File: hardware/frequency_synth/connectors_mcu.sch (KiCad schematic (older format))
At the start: 0 parts

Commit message: finished initial schematic of synth module
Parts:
- added D?: LED, LEDs:LED_0603, symbol LED
- added P? (x2): CONN_01X02, Terminal_Blocks:TerminalBlock_Pheonix_PT-3.5mm_2pol, symbol CONN_01X02
- added R?: 10k, Resistors_SMD:R_0603, symbol R_Small
- added U?: boosterpack_ti, vna_footprints:ti_booster40, symbol boosterpack_ti
- added U?: CONN_SMA, vna_footprints:732512200_SMA, symbol CONN_SMA
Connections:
- net labels added: +3V3, +5V, 3V3, 5V, ADF_CE_0, ADF_CLK_0, ADF_DATA_0, ADF_LE_0, ADF_LOCK_0, ATT_1, ATT_2, ATT_3, ATT_4, ATT_5, ATT_6, FILTA, FILTA_0, FILTB, FILTB_0, FILTC, FILTC_0, GND, LMX_CE, LMX_CLK, LMX_DAT, LMX_LE, LMX_LOCK, POWERDET, REF_CE, REF_OE, REF_SCL, REF_SDA, RFSW, RFSW_0, RFSW_1, RFSW_2, SYNTH_OUT, VCC
- wire segments 0 -> 64
- no-connect marks 0 -> 2
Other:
- note added: "filter bank"
- note added: "rf switch control"

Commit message: reducing component values across module, synth schematic cleanups
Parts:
- removed U?: CONN_SMA, vna_footprints:732512200_SMA, symbol CONN_SMA
- added U?: CONN_SMA_2GND, symbol CONN_SMA_2GND
- R55: renamed from R?; footprint Resistors_SMD:R_0603 -> Resistors_SMD:R_0402
- gave numbers to parts that had none: 4
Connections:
- wire segments 64 -> 62
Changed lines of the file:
@@
 LIBS:74hc04
 LIBS:74hc04_full
+LIBS:conn_sma_2gnd
 LIBS:frequency_synth-cache
-LIBS:boosterpack-cache
-LIBS:refclk_breakout-cache
 EELAYER 25 0
 EELAYER END
@@
 $EndDescr
 $Comp
-L boosterpack_ti U?
+L boosterpack_ti U17
 U 1 1 572E0ED9
 P 1950 2850
-F 0 "U?" H 1700 4450 60  0000 C CNN
+F 0 "U17" H 1700 4450 60  0000 C CNN
 F 1 "boosterpack_ti" H 1950 4250 60  0000 C CNN
 F 2 "vna_footprints:ti_booster40" H 1700 4450 60  0001 C CNN
@@
 $EndComp
 $Comp
-L GND #PWR?
+L GND #PWR213
 U 1 1 572E0EDA
 P 2650 2950
-F 0 "#PWR?" H 2650 2700 50  0001 C CNN
+F 0 "#PWR213" H 2650 2700 50  0001 C CNN
 F 1 "GND" H 2650 2800 50  0000 C CNN
 F 2 "" H 2650 2950 50  0000 C CNN
@@
 $EndComp
 $Comp
-L GND #PWR?
+L GND #PWR214
 U 1 1 572E0EDB
 P 2700 1850
-F 0 "#PWR?" H 2700 1600 50  0001 C CNN
+F 0 "#PWR214" H 2700 1600 50  0001 C CNN
 F 1 "GND" H 2700 1700 50  0000 C CNN
 F 2 "" H 2700 1850 50  0000 C CNN
@@
 $EndComp
 $Comp
-L CONN_01X02 P?
+L CONN_01X02 P1
 U 1 1 572E0EDE
 P 6050 1150
-F 0 "P?" H 6050 1300 50  0000 C CNN
+F 0 "P1" H 6050 1300 50  0000 C CNN
 F 1 "CONN_01X02" V 6150 1150 50  0000 C CNN
 F 2 "Terminal_Blocks:TerminalBlock_Pheonix_PT-3.5mm_2pol" H 6050 1150 50  0001 C CNN
@@
 $EndComp
 $Comp
-L GND #PWR?
+L GND #PWR218
 U 1 1 572E0EDF
 P 6000 1450
-F 0 "#PWR?" H 6000 1200 50  0001 C CNN
+F 0 "#PWR218" H 6000 1200 50  0001 C CNN
 F 1 "GND" H 6000 1300 50  0000 C CNN
 F 2 "" H 6000 1450 50  0000 C CNN
@@
 FILTC_0
 $Comp
-L GND #PWR?
+L GND #PWR222
 U 1 1 572E0EEC
 P 9800 1200
-F 0 "#PWR?" H 9800 950 50  0001 C CNN
+F 0 "#PWR222" H 9800 950 50  0001 C CNN
 F 1 "GND" H 9800 1050 50  0000 C CNN
 F 2 "" H 9800 1200 50  0000 C CNN
@@
 $EndComp
 $Comp
-L +5V #PWR?
+L +5V #PWR223
 U 1 1 572E0EEE
 P 9850 1300
-F 0 "#PWR?" H 9850 1150 50  0001 C CNN
+F 0 "#PWR223" H 9850 1150 50  0001 C CNN
 F 1 "+5V" H 9850 1440 50  0000 C CNN
 F 2 "" H 9850 1300 50  0000 C CNN
@@
 FILTC_0
 $Comp
-L LED D?
+L LED D9
 U 1 1 572E0F0F
 P 5300 1100
-F 0 "D?" H 5300 1200 50  0000 C CNN
+F 0 "D9" H 5300 1200 50  0000 C CNN
 F 1 "LED" H 5300 1000 50  0000 C CNN
 F 2 "LEDs:LED_0603" H 5300 1100 50  0001 C CNN
@@
 $EndComp
 $Comp
-L R_Small R?
+L R_Small R55
 U 1 1 572E0F10
 P 5300 1500
-F 0 "R?" H 5330 1520 50  0000 L CNN
+F 0 "R55" H 5330 1520 50  0000 L CNN
 F 1 "10k" H 5330 1460 50  0000 L CNN
-F 2 "Resistors_SMD:R_0603" H 5300 1500 50  0001 C CNN
+F 2 "Resistors_SMD:R_0402" H 5300 1500 50  0001 C CNN
 F 3 "" H 5300 1500 50  0000 C CNN
 	1    5300 1500
@@
 $EndComp
 $Comp
-L VCC #PWR?
+L VCC #PWR216
 U 1 1 572E0F11
 P 5300 800
-F 0 "#PWR?" H 5300 650 50  0001 C CNN
+F 0 "#PWR216" H 5300 650 50  0001 C CNN
 F 1 "VCC" H 5300 950 50  0000 C CNN
 F 2 "" H 5300 800 50  0000 C CNN
@@
 $EndComp
 $Comp
-L GND #PWR?
+L GND #PWR217
 U 1 1 572E0F12
 P 5300 1700
-F 0 "#PWR?" H 5300 1450 50  0001 C CNN
+F 0 "#PWR217" H 5300 1450 50  0001 C CNN
 F 1 "GND" H 5300 1550 50  0000 C CNN
 F 2 "" H 5300 1700 50  0000 C CNN
@@
 POWERDET
 $Comp
-L CONN_SMA U?
-U 1 1 572E0F13
-P 4700 4700
-F 0 "U?" H 4350 4900 60  0000 C CNN
-F 1 "CONN_SMA" H 4550 5050 60  0000 C CNN
-F 2 "vna_footprints:732512200_SMA" H 4700 4700 60  0001 C CNN
-F 3 "" H 4700 4700 60  0000 C CNN
-	1    4700 4700
-	1    0    0    -1
-$EndComp
-$Comp
-L GND #PWR?
+L GND #PWR215
 U 1 1 572E0F14
 P 4550 5300
-F 0 "#PWR?" H 4550 5050 50  0001 C CNN
+F 0 "#PWR215" H 4550 5050 50  0001 C CNN
 F 1 "GND" H 4550 5150 50  0000 C CNN
 F 2 "" H 4550 5300 50  0000 C CNN
@@
 Text HLabel 3400 4700 0    60   Input ~ 0
 SYNTH_OUT
-Connection ~ 4750 5250
-Wire Wire Line
-	4750 5150 4750 5250
-Connection ~ 4650 5250
 Wire Wire Line
 	4650 5150 4650 5250
 Connection ~ 4550 5250
 Wire Wire Line
-	4550 5250 4850 5250
-Wire Wire Line
-	4850 5250 4850 5150
-Wire Wire Line
 	4550 5150 4550 5300
 Wire Wire Line
-	3400 4700 4150 4700
+	3400 4700 4200 4700
 Wire Wire Line
 	2550 1950 3000 1950
@@
 3V3
 $Comp
-L +3V3 #PWR?
+L +3V3 #PWR224
 U 1 1 5730B3CA
 P 9850 1400
-F 0 "#PWR?" H 9850 1250 50  0001 C CNN
+F 0 "#PWR224" H 9850 1250 50  0001 C CNN
 F 1 "+3V3" H 9850 1540 50  0000 C CNN
 F 2 "" H 9850 1400 50  0000 C CNN
@@
 NoConn ~ 1250 1750
 $Comp
-L +3V3 #PWR?
+L +3V3 #PWR220
 U 1 1 573281E3
 P 6500 1100
-F 0 "#PWR?" H 6500 950 50  0001 C CNN
+F 0 "#PWR220" H 6500 950 50  0001 C CNN
 F 1 "+3V3" H 6500 1240 50  0000 C CNN
 F 2 "" H 6500 1100 50  0000 C CNN
@@
 $EndComp
 $Comp
-L CONN_01X02 P?
+L CONN_01X02 P2
 U 1 1 573282FD
 P 6100 2000
-F 0 "P?" H 6100 2150 50  0000 C CNN
+F 0 "P2" H 6100 2150 50  0000 C CNN
 F 1 "CONN_01X02" V 6200 2000 50  0000 C CNN
 F 2 "Terminal_Blocks:TerminalBlock_Pheonix_PT-3.5mm_2pol" H 6100 2000 50  0001 C CNN
@@
 $EndComp
 $Comp
-L GND #PWR?
+L GND #PWR219
 U 1 1 57328303
 P 6050 2300
-F 0 "#PWR?" H 6050 2050 50  0001 C CNN
+F 0 "#PWR219" H 6050 2050 50  0001 C CNN
 F 1 "GND" H 6050 2150 50  0000 C CNN
 F 2 "" H 6050 2300 50  0000 C CNN
@@
 	6050 2200 6050 2300
 $Comp
-L +5V #PWR?
+L +5V #PWR221
 U 1 1 57328345
 P 6550 1950
-F 0 "#PWR?" H 6550 1800 50  0001 C CNN
+F 0 "#PWR221" H 6550 1800 50  0001 C CNN
 F 1 "+5V" H 6550 2090 50  0000 C CNN
 F 2 "" H 6550 1950 50  0000 C CNN
@@
 	1    0    0    -1
 $EndComp
+$Comp
+L CONN_SMA_2GND U?
+U 1 1 572C89B0
+P 4600 4700
+F 0 "U?" H 4300 4900 60  0000 C CNN
+F 1 "CONN_SMA_2GND" H 4650 5000 60  0000 C CNN
+F 2 "" H 4600 4700 60  0000 C CNN
+F 3 "" H 4600 4700 60  0000 C CNN
+	1    4600 4700
+	-1   0    0    -1
+$EndComp
+Wire Wire Line
+	4650 5250 4550 5250
 $EndSCHEMATC

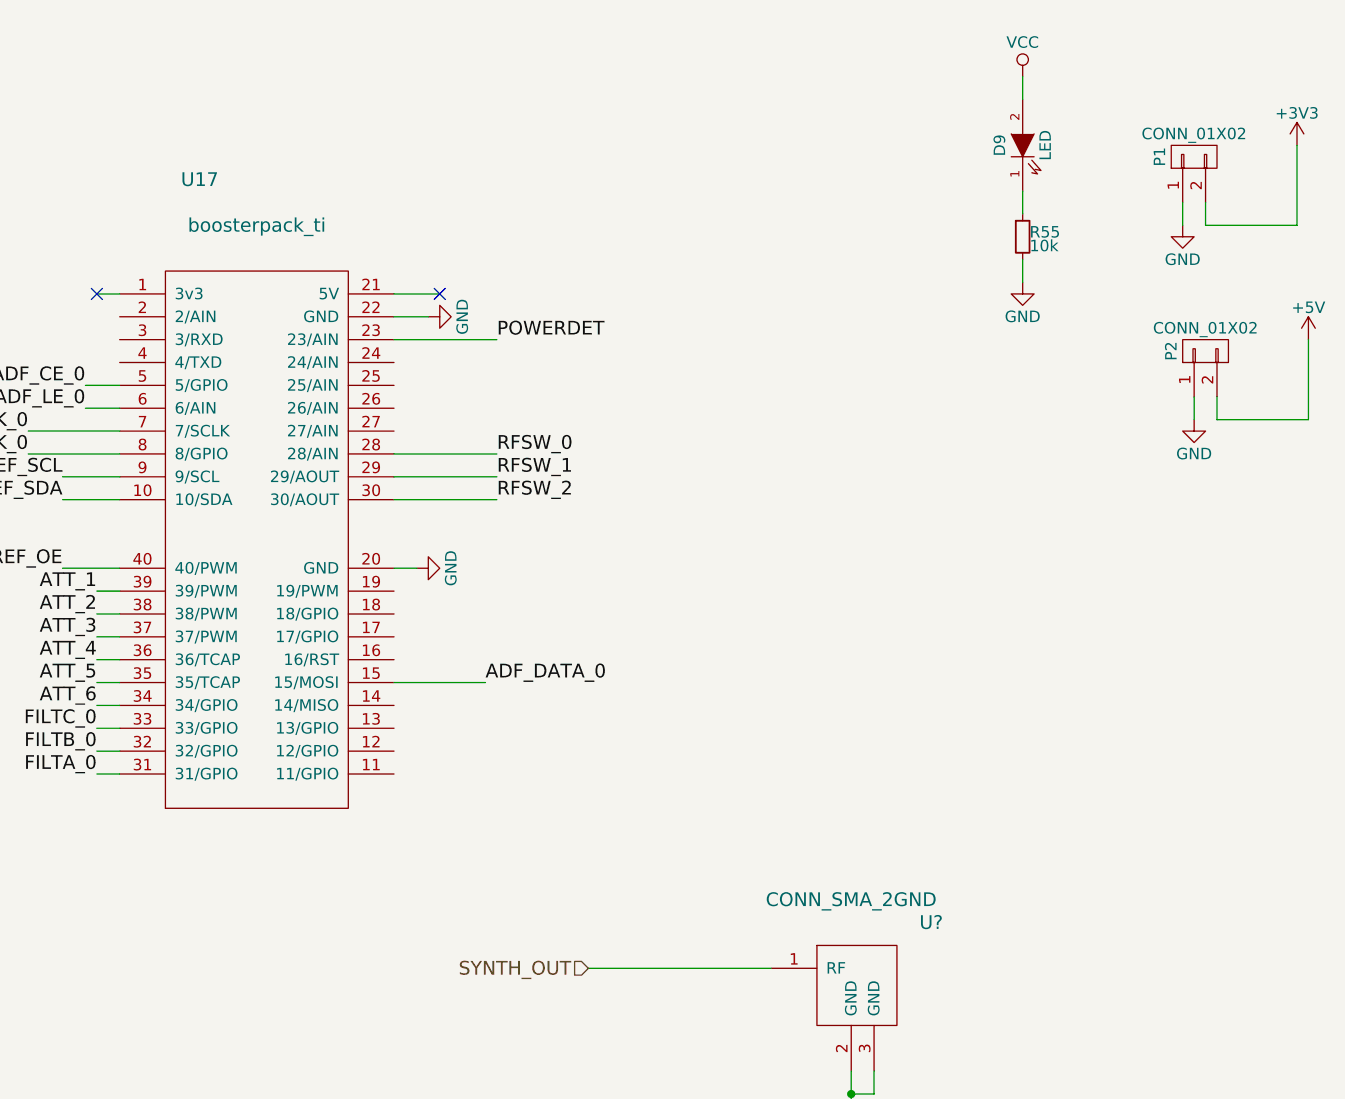
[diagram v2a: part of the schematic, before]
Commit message: started on component placement
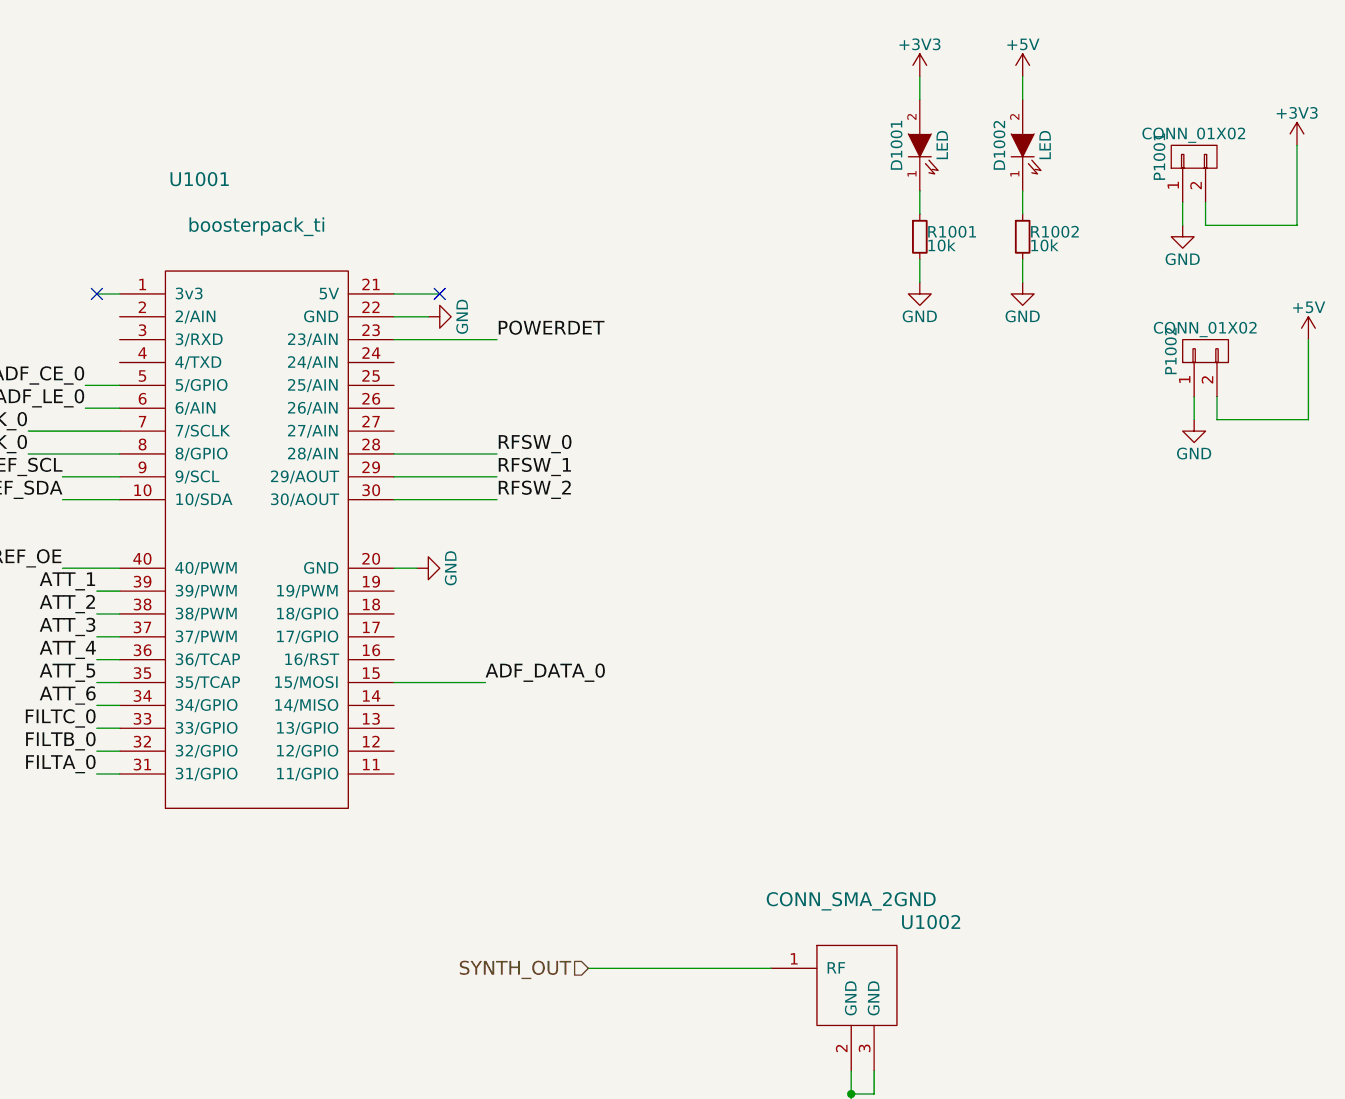
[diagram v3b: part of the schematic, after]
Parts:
- added D1001: LED, LEDs:LED_0603, symbol LED
- added R1001: 10k, Resistors_SMD:R_0402, symbol R_Small
- U1002: renamed from U?; footprint (none) -> vna_footprints:142-0721-882_sma_cutout
- renumbered D9 to D1002, P1 to P1001, P2 to P1002, R55 to R1002, U17 to U1001
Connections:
- net VCC is gone; now on net +5V: D1002.2 (A)
- net +3V3: now also D1001.2 (A)
- net GND: now also R1001.2
- new net: D1001.1 (K), R1001.1
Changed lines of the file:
@@
 $EndDescr
 $Comp
-L boosterpack_ti U17
+L boosterpack_ti U1001
 U 1 1 572E0ED9
 P 1950 2850
-F 0 "U17" H 1700 4450 60  0000 C CNN
+F 0 "U1001" H 1700 4450 60  0000 C CNN
 F 1 "boosterpack_ti" H 1950 4250 60  0000 C CNN
 F 2 "vna_footprints:ti_booster40" H 1700 4450 60  0001 C CNN
@@
 $EndComp
 $Comp
-L GND #PWR213
+L GND #PWR0207
 U 1 1 572E0EDA
 P 2650 2950
-F 0 "#PWR213" H 2650 2700 50  0001 C CNN
+F 0 "#PWR0207" H 2650 2700 50  0001 C CNN
 F 1 "GND" H 2650 2800 50  0000 C CNN
 F 2 "" H 2650 2950 50  0000 C CNN
@@
 $EndComp
 $Comp
-L GND #PWR214
+L GND #PWR0208
 U 1 1 572E0EDB
 P 2700 1850
-F 0 "#PWR214" H 2700 1600 50  0001 C CNN
+F 0 "#PWR0208" H 2700 1600 50  0001 C CNN
 F 1 "GND" H 2700 1700 50  0000 C CNN
 F 2 "" H 2700 1850 50  0000 C CNN
@@
 $EndComp
 $Comp
-L CONN_01X02 P1
+L CONN_01X02 P1001
 U 1 1 572E0EDE
 P 6050 1150
-F 0 "P1" H 6050 1300 50  0000 C CNN
+F 0 "P1001" H 6050 1300 50  0000 C CNN
 F 1 "CONN_01X02" V 6150 1150 50  0000 C CNN
 F 2 "Terminal_Blocks:TerminalBlock_Pheonix_PT-3.5mm_2pol" H 6050 1150 50  0001 C CNN
@@
 $EndComp
 $Comp
-L GND #PWR218
+L GND #PWR0209
 U 1 1 572E0EDF
 P 6000 1450
-F 0 "#PWR218" H 6000 1200 50  0001 C CNN
+F 0 "#PWR0209" H 6000 1200 50  0001 C CNN
 F 1 "GND" H 6000 1300 50  0000 C CNN
 F 2 "" H 6000 1450 50  0000 C CNN
@@
 FILTC_0
 $Comp
-L GND #PWR222
+L GND #PWR0210
 U 1 1 572E0EEC
 P 9800 1200
-F 0 "#PWR222" H 9800 950 50  0001 C CNN
+F 0 "#PWR0210" H 9800 950 50  0001 C CNN
 F 1 "GND" H 9800 1050 50  0000 C CNN
 F 2 "" H 9800 1200 50  0000 C CNN
@@
 $EndComp
 $Comp
-L +5V #PWR223
+L +5V #PWR0211
 U 1 1 572E0EEE
 P 9850 1300
-F 0 "#PWR223" H 9850 1150 50  0001 C CNN
+F 0 "#PWR0211" H 9850 1150 50  0001 C CNN
 F 1 "+5V" H 9850 1440 50  0000 C CNN
 F 2 "" H 9850 1300 50  0000 C CNN
@@
 FILTC_0
 $Comp
-L LED D9
+L LED D1002
 U 1 1 572E0F0F
 P 5300 1100
-F 0 "D9" H 5300 1200 50  0000 C CNN
+F 0 "D1002" H 5300 1200 50  0000 C CNN
 F 1 "LED" H 5300 1000 50  0000 C CNN
 F 2 "LEDs:LED_0603" H 5300 1100 50  0001 C CNN
@@
 $EndComp
 $Comp
-L R_Small R55
+L R_Small R1002
 U 1 1 572E0F10
 P 5300 1500
-F 0 "R55" H 5330 1520 50  0000 L CNN
+F 0 "R1002" H 5330 1520 50  0000 L CNN
 F 1 "10k" H 5330 1460 50  0000 L CNN
 F 2 "Resistors_SMD:R_0402" H 5300 1500 50  0001 C CNN
@@
 $EndComp
 $Comp
-L VCC #PWR216
-U 1 1 572E0F11
-P 5300 800
-F 0 "#PWR216" H 5300 650 50  0001 C CNN
-F 1 "VCC" H 5300 950 50  0000 C CNN
-F 2 "" H 5300 800 50  0000 C CNN
-F 3 "" H 5300 800 50  0000 C CNN
-	1    5300 800
-	1    0    0    -1
-$EndComp
-$Comp
-L GND #PWR217
+L GND #PWR0212
 U 1 1 572E0F12
 P 5300 1700
-F 0 "#PWR217" H 5300 1450 50  0001 C CNN
+F 0 "#PWR0212" H 5300 1450 50  0001 C CNN
 F 1 "GND" H 5300 1550 50  0000 C CNN
 F 2 "" H 5300 1700 50  0000 C CNN
@@
 POWERDET
 $Comp
-L GND #PWR215
+L GND #PWR0213
 U 1 1 572E0F14
 P 4550 5300
-F 0 "#PWR215" H 4550 5050 50  0001 C CNN
+F 0 "#PWR0213" H 4550 5050 50  0001 C CNN
 F 1 "GND" H 4550 5150 50  0000 C CNN
 F 2 "" H 4550 5300 50  0000 C CNN
@@
 3V3
 $Comp
-L +3V3 #PWR224
+L +3V3 #PWR0214
 U 1 1 5730B3CA
 P 9850 1400
-F 0 "#PWR224" H 9850 1250 50  0001 C CNN
+F 0 "#PWR0214" H 9850 1250 50  0001 C CNN
 F 1 "+3V3" H 9850 1540 50  0000 C CNN
 F 2 "" H 9850 1400 50  0000 C CNN
@@
 NoConn ~ 1250 1750
 $Comp
-L +3V3 #PWR220
+L +3V3 #PWR0215
 U 1 1 573281E3
 P 6500 1100
-F 0 "#PWR220" H 6500 950 50  0001 C CNN
+F 0 "#PWR0215" H 6500 950 50  0001 C CNN
 F 1 "+3V3" H 6500 1240 50  0000 C CNN
 F 2 "" H 6500 1100 50  0000 C CNN
@@
 $EndComp
 $Comp
-L CONN_01X02 P2
+L CONN_01X02 P1002
 U 1 1 573282FD
 P 6100 2000
-F 0 "P2" H 6100 2150 50  0000 C CNN
+F 0 "P1002" H 6100 2150 50  0000 C CNN
 F 1 "CONN_01X02" V 6200 2000 50  0000 C CNN
 F 2 "Terminal_Blocks:TerminalBlock_Pheonix_PT-3.5mm_2pol" H 6100 2000 50  0001 C CNN
@@
 $EndComp
 $Comp
-L GND #PWR219
+L GND #PWR0216
 U 1 1 57328303
 P 6050 2300
-F 0 "#PWR219" H 6050 2050 50  0001 C CNN
+F 0 "#PWR0216" H 6050 2050 50  0001 C CNN
 F 1 "GND" H 6050 2150 50  0000 C CNN
 F 2 "" H 6050 2300 50  0000 C CNN
@@
 	6050 2200 6050 2300
 $Comp
-L +5V #PWR221
+L +5V #PWR0217
 U 1 1 57328345
 P 6550 1950
-F 0 "#PWR221" H 6550 1800 50  0001 C CNN
+F 0 "#PWR0217" H 6550 1800 50  0001 C CNN
 F 1 "+5V" H 6550 2090 50  0000 C CNN
 F 2 "" H 6550 1950 50  0000 C CNN
@@
 $EndComp
 $Comp
-L CONN_SMA_2GND U?
+L CONN_SMA_2GND U1002
 U 1 1 572C89B0
 P 4600 4700
-F 0 "U?" H 4300 4900 60  0000 C CNN
+F 0 "U1002" H 4300 4900 60  0000 C CNN
 F 1 "CONN_SMA_2GND" H 4650 5000 60  0000 C CNN
-F 2 "" H 4600 4700 60  0000 C CNN
+F 2 "vna_footprints:142-0721-882_sma_cutout" H 4600 4700 60  0001 C CNN
 F 3 "" H 4600 4700 60  0000 C CNN
 	1    4600 4700
@@
 Wire Wire Line
 	4650 5250 4550 5250
+$Comp
+L +5V #PWR0218
+U 1 1 572C5D1D
+P 5300 800
+F 0 "#PWR0218" H 5300 650 50  0001 C CNN
+F 1 "+5V" H 5300 940 50  0000 C CNN
+F 2 "" H 5300 800 50  0000 C CNN
+F 3 "" H 5300 800 50  0000 C CNN
+	1    5300 800
+	1    0    0    -1
+$EndComp
+$Comp
+L LED D1001
+U 1 1 572C5E57
+P 4850 1100
+F 0 "D1001" H 4850 1200 50  0000 C CNN
+F 1 "LED" H 4850 1000 50  0000 C CNN
+F 2 "LEDs:LED_0603" H 4850 1100 50  0001 C CNN
+F 3 "" H 4850 1100 50  0000 C CNN
+	1    4850 1100
+	0    -1   -1   0
+$EndComp
+$Comp
+L R_Small R1001
+U 1 1 572C5E5D
+P 4850 1500
+F 0 "R1001" H 4880 1520 50  0000 L CNN
+F 1 "10k" H 4880 1460 50  0000 L CNN
+F 2 "Resistors_SMD:R_0402" H 4850 1500 50  0001 C CNN
+F 3 "" H 4850 1500 50  0000 C CNN
+	1    4850 1500
+	1    0    0    -1
+$EndComp
+$Comp
+L GND #PWR0219
+U 1 1 572C5E63
+P 4850 1700
+F 0 "#PWR0219" H 4850 1450 50  0001 C CNN
+F 1 "GND" H 4850 1550 50  0000 C CNN
+F 2 "" H 4850 1700 50  0000 C CNN
+F 3 "" H 4850 1700 50  0000 C CNN
+	1    4850 1700
+	1    0    0    -1
+$EndComp
+Wire Wire Line
+	4850 1700 4850 1600
+Wire Wire Line
+	4850 1300 4850 1400
+Wire Wire Line
+	4850 800  4850 900
+$Comp
+L +3V3 #PWR0220
+U 1 1 572C5EF3
+P 4850 800
+F 0 "#PWR0220" H 4850 650 50  0001 C CNN
+F 1 "+3V3" H 4850 940 50  0000 C CNN
+F 2 "" H 4850 800 50  0000 C CNN
+F 3 "" H 4850 800 50  0000 C CNN
+	1    4850 800
+	1    0    0    -1
+$EndComp
 $EndSCHEMATC
